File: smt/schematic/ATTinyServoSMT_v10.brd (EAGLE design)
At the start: 27.9 x 29.2 mm, 12 parts, among them U1 ATTINY85-20PU, Y1 RESONATORPTH

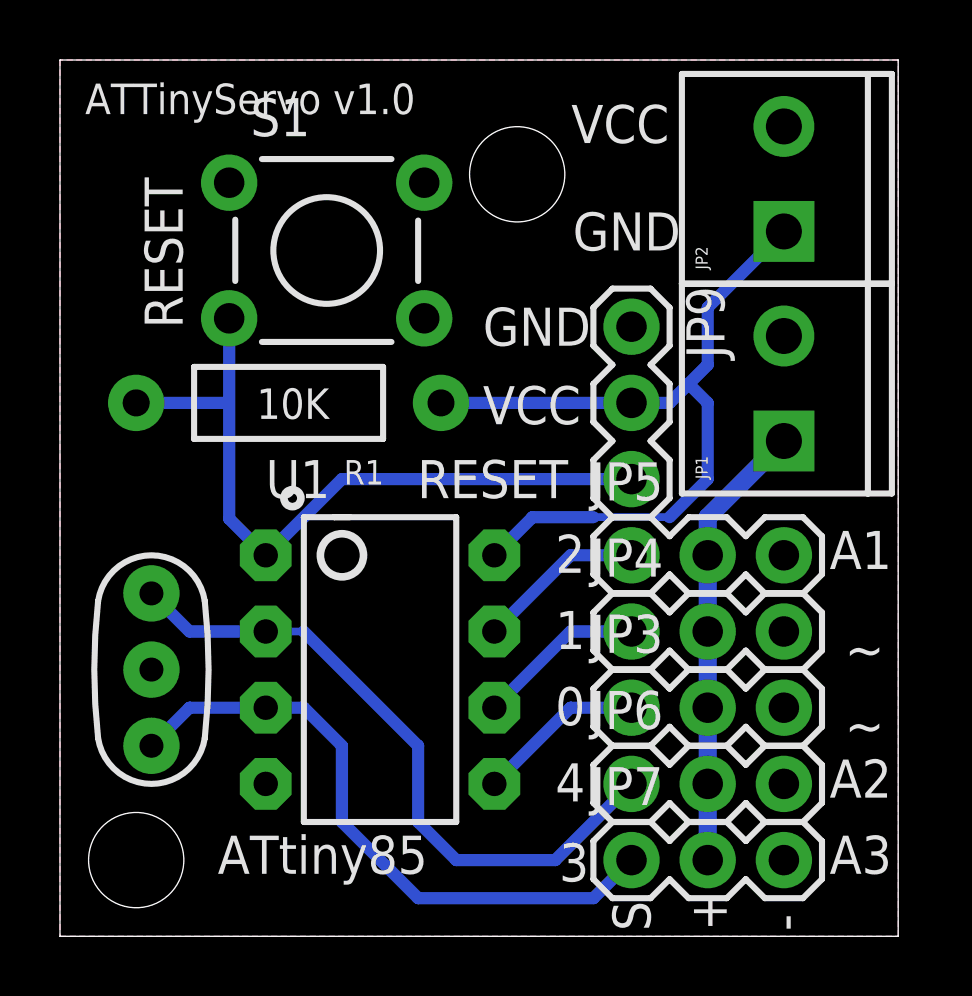
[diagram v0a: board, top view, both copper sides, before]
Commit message: Added programming, packaging, updated through hole version, and new smt version.
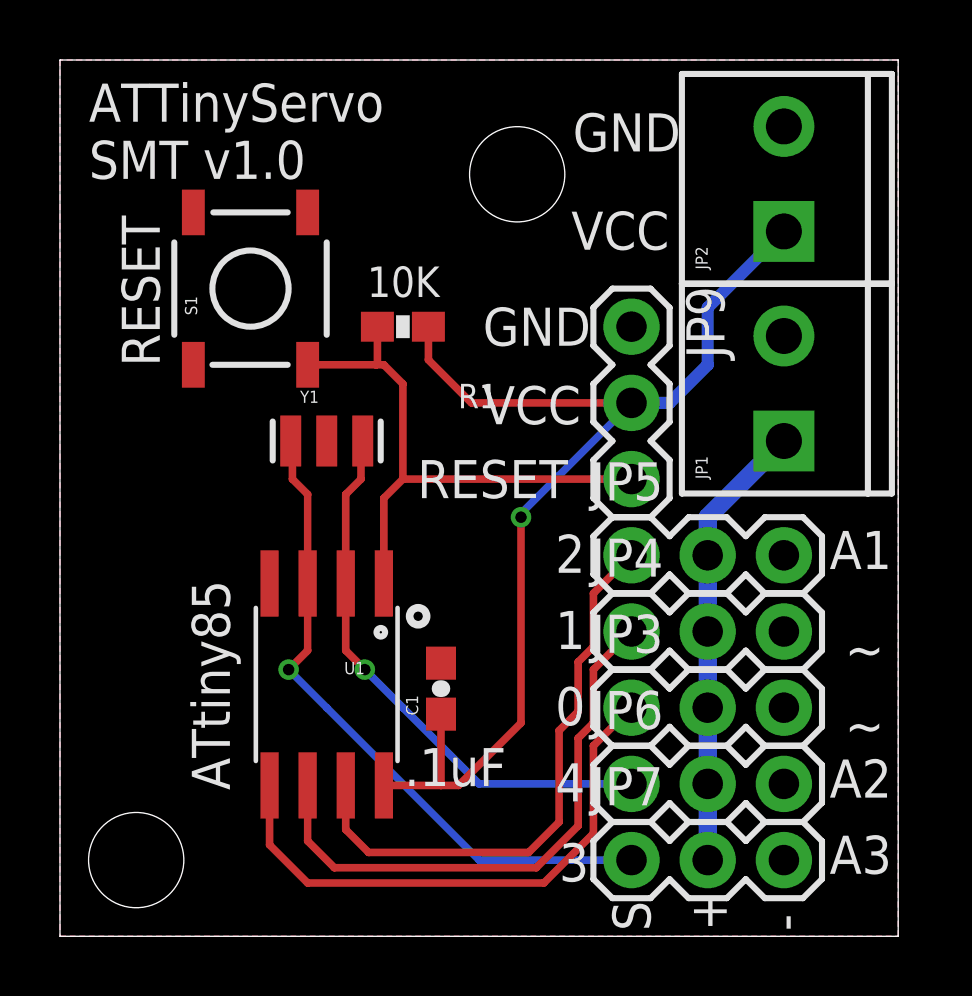
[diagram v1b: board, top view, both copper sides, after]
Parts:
- added C1: .1uF, SparkFun-Capacitors:0603-CAP
- R1: device SparkFun:AXIAL-0.4 -> SparkFun:0603-RES
- S1: device SparkFun:TACTILE-PTH -> SparkFun:TACTILE_SWITCH_SMD
- U1: device SparkFun:DIP08 -> SparkFun:SO08-EIAJ
- Y1: value RESONATORPTH -> RESONATORSMD; device SparkFun:RESONATOR-PTH -> SparkFun:RESONATOR-SMD
- moved Y1 9.60 mm to (8.89, 16.5), turned to 0 degrees
- moved R1 4.58 mm to (11.4, 20.3)
- moved S1 2.84 mm to (6.35, 21.6), turned to 90 degrees
- moved U1 1.85 mm to (8.89, 8.38), turned to 180 degrees
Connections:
- net GND: now also C1.2
- net RESET: now also R1.2; no longer R1.P$2
- net VCC: now also C1.1, R1.1; no longer R1.P$1
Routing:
- net N$7: track 5.62 -> 19.2 mm
- net N$8: track 5.62 -> 19.0 mm
- net N$9: track 5.62 -> 18.7 mm
- net VCC: track 26.5 -> 37.0 mm, vias 0 -> 1
- net RESET: track 24.8 -> 19.3 mm
- net N$2: track 22.2 -> 18.6 mm, vias 0 -> 1
- net N$3: track 21.2 -> 22.2 mm, vias 0 -> 1
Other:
- board text added: ".1uF"
- board text added: "ATTinyServo SMT v1.0"
- board text removed: "ATTinyServo v1.0"
